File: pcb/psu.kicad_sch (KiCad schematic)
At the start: 20 parts, among them IC3 TPS561243DRLR, IC4 TPS561243DRLR, J1 Conn_01x02_Socket

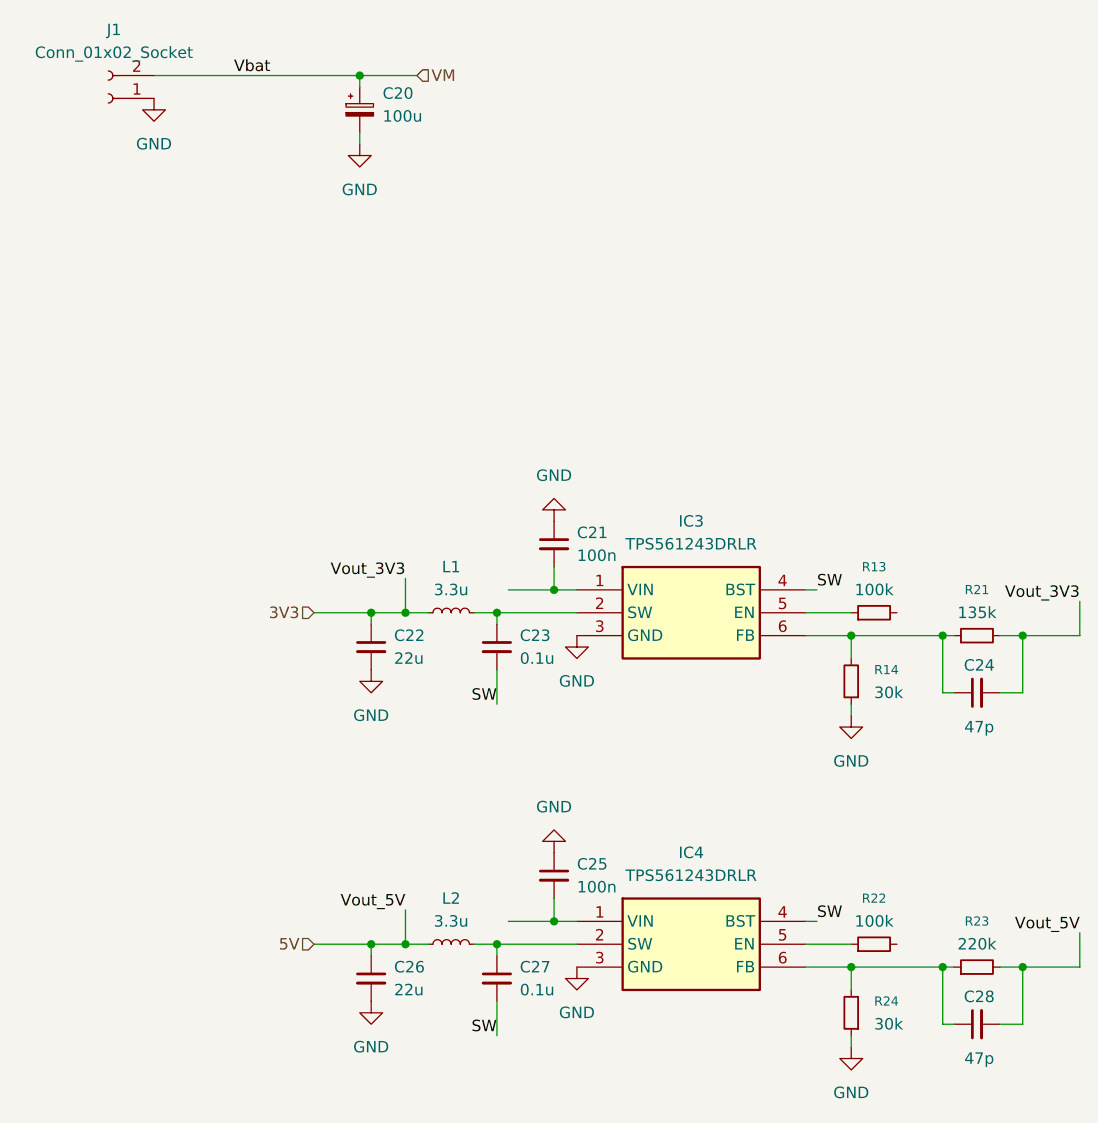
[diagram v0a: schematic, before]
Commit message: driver and buck converter layout
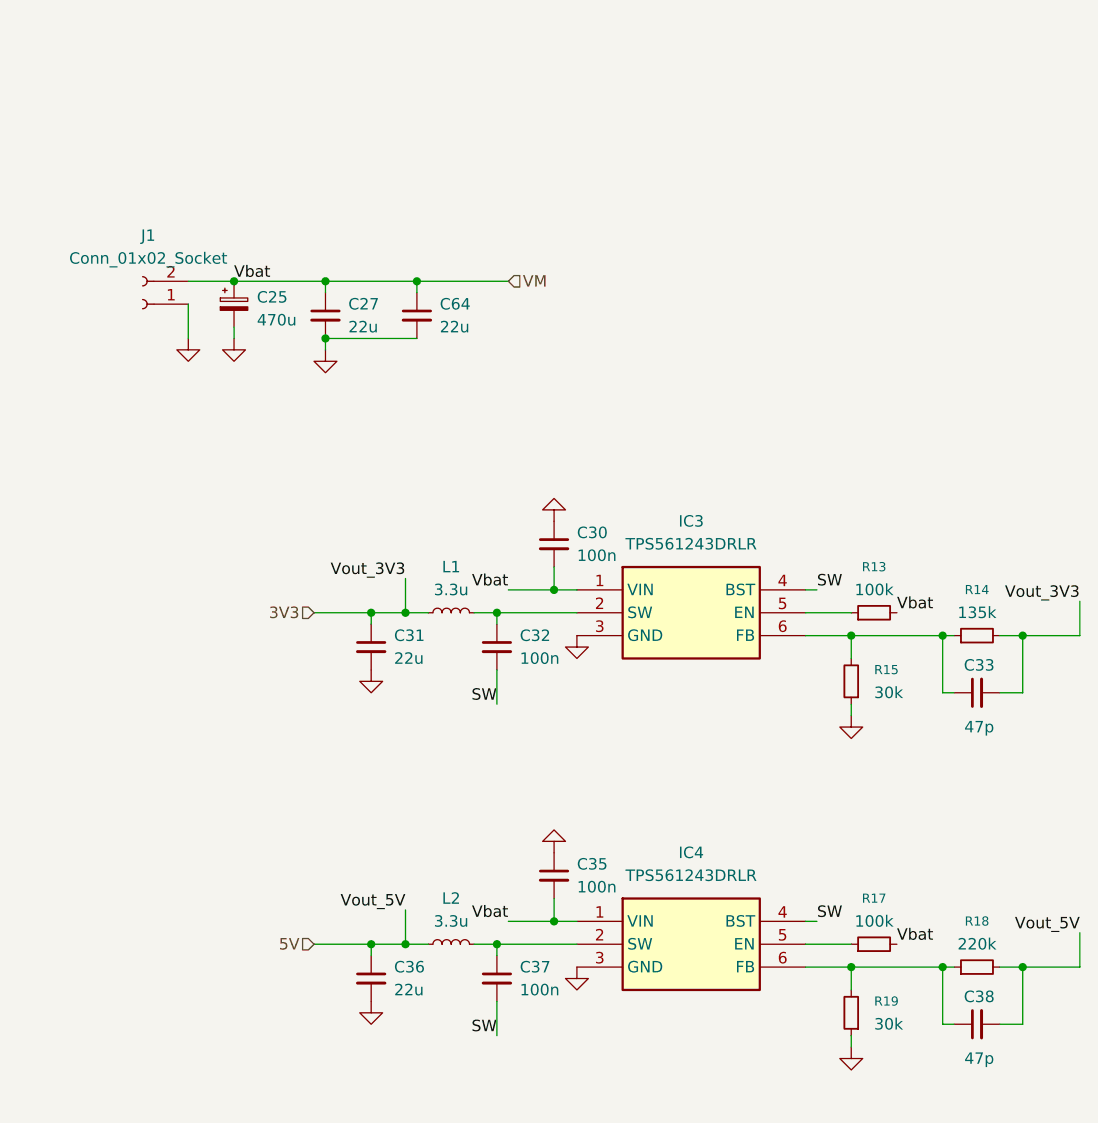
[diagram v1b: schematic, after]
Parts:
- added C27, C64: 22u, Capacitor_SMD:C_0603_1608Metric, symbol Device:C_Small
- C25: renamed from C20; value 100u -> 470u; footprint (none) -> Capacitor_THT:C_Radial_D10.0mm_H16.0mm_P5.00mm
- C30: renamed from C21; footprint (none) -> Capacitor_SMD:C_0603_1608Metric
- C31: renamed from C22; footprint (none) -> Capacitor_SMD:C_0805_2012Metric
- C32: renamed from C23; value 0.1u -> 100n; footprint (none) -> Capacitor_SMD:C_0603_1608Metric
- C33: renamed from C24; footprint (none) -> Capacitor_SMD:C_0603_1608Metric
- C35: renamed from C25; footprint (none) -> Capacitor_SMD:C_0603_1608Metric
- C36: renamed from C26; footprint (none) -> Capacitor_SMD:C_0805_2012Metric
- C37: renamed from C27; value 0.1u -> 100n; footprint (none) -> Capacitor_SMD:C_0603_1608Metric
- C38: renamed from C28; footprint (none) -> Capacitor_SMD:C_0603_1608Metric
- IC3, IC4: footprint SOTFL50P160X60-6N -> TPS561243:SOTFL50P160X60-6N
- J1: footprint (none) -> Connector_AMASS:AMASS_XT60-M_1x02_P7.20mm_Vertical
- L1, L2: footprint (none) -> Inductor_SMD:L_1008_2520Metric
- R13: footprint (none) -> Resistor_SMD:R_0603_1608Metric
- R14: renamed from R21; footprint (none) -> Resistor_SMD:R_0603_1608Metric
- R15: renamed from R14; footprint (none) -> Resistor_SMD:R_0603_1608Metric
- R17: renamed from R22; footprint (none) -> Resistor_SMD:R_0603_1608Metric
- R18: renamed from R23; footprint (none) -> Resistor_SMD:R_0603_1608Metric
- R19: renamed from R24; footprint (none) -> Resistor_SMD:R_0603_1608Metric
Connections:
- net GND: now also C27.2, C64.2
- net VM: now also C30.2, C35.2, IC3.1 (VIN), IC4.1 (VIN), R13.2, R17.2, C27.1, C64.1
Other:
- moved on the sheet: C25, J1

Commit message: routing
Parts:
- J1: footprint Connector_AMASS:AMASS_XT60-M_1x02_P7.20mm_Vertical -> Connector_AMASS:AMASS_XT60PW-M_1x02_P7.20mm_Horizontal
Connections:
- net SW renamed SW3V3
- net SW3V3: no longer C37.2, IC4.4 (BST)
- new net SW5V: C37.2, IC4.4 (BST)
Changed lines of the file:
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@@
-		)
-	)
-	(label "SW"
-		(at 77.47 109.22 180)
-		(effects
-			(font
-				(size 1.27 1.27)
-			)
-			(justify right bottom)
 		)
 	)
@@
 		)
 	)
-	(label "SW"
+	(label "SW5V"
 		(at 113.03 133.35 0)
 		(effects
@@
 		)
 	)
-	(label "SW"
+	(label "SW3V3"
 		(at 113.03 96.52 0)
 		(effects
@@
 		)
 	)
-	(label "SW"
-		(at 77.47 146.05 180)
+	(label "SW5V"
+		(at 77.47 146.05 0)
 		(effects
 			(font
 				(size 1.27 1.27)
 			)
-			(justify right bottom)
+			(justify left bottom)
+		)
+	)
+	(label "SW3V3"
+		(at 77.47 109.22 0)
+		(effects
+			(font
+				(size 1.27 1.27)
+			)
+			(justify left bottom)
 		)
 	)
@@
 		(lib_id "Device:C_Small")
 		(at 83.82 128.27 0)
-		(unit 1)
-		(exclude_from_sim no)
-		(in_bom yes)
-		(on_board yes)
-		(dnp no)
-		(fields_autoplaced yes)
+		(mirror y)
+		(unit 1)
+		(exclude_from_sim no)
+		(in_bom yes)
+		(on_board yes)
+		(dnp no)
 		(property "Reference" "C35"
-			(at 86.36 127.0062 0)
+			(at 81.28 127.0062 0)
 			(effects
 				(font
@@
 		)
 		(property "Value" "100n"
-			(at 86.36 129.5462 0)
+			(at 81.28 129.5462 0)
 			(effects
 				(font
@@
 			)
 		)
-		(property "Footprint" "Connector_AMASS:AMASS_XT60-M_1x02_P7.20mm_Vertical"
+		(property "Footprint" "Connector_AMASS:AMASS_XT60PW-M_1x02_P7.20mm_Horizontal"
 			(at 38.1 64.77 0)
 			(effects

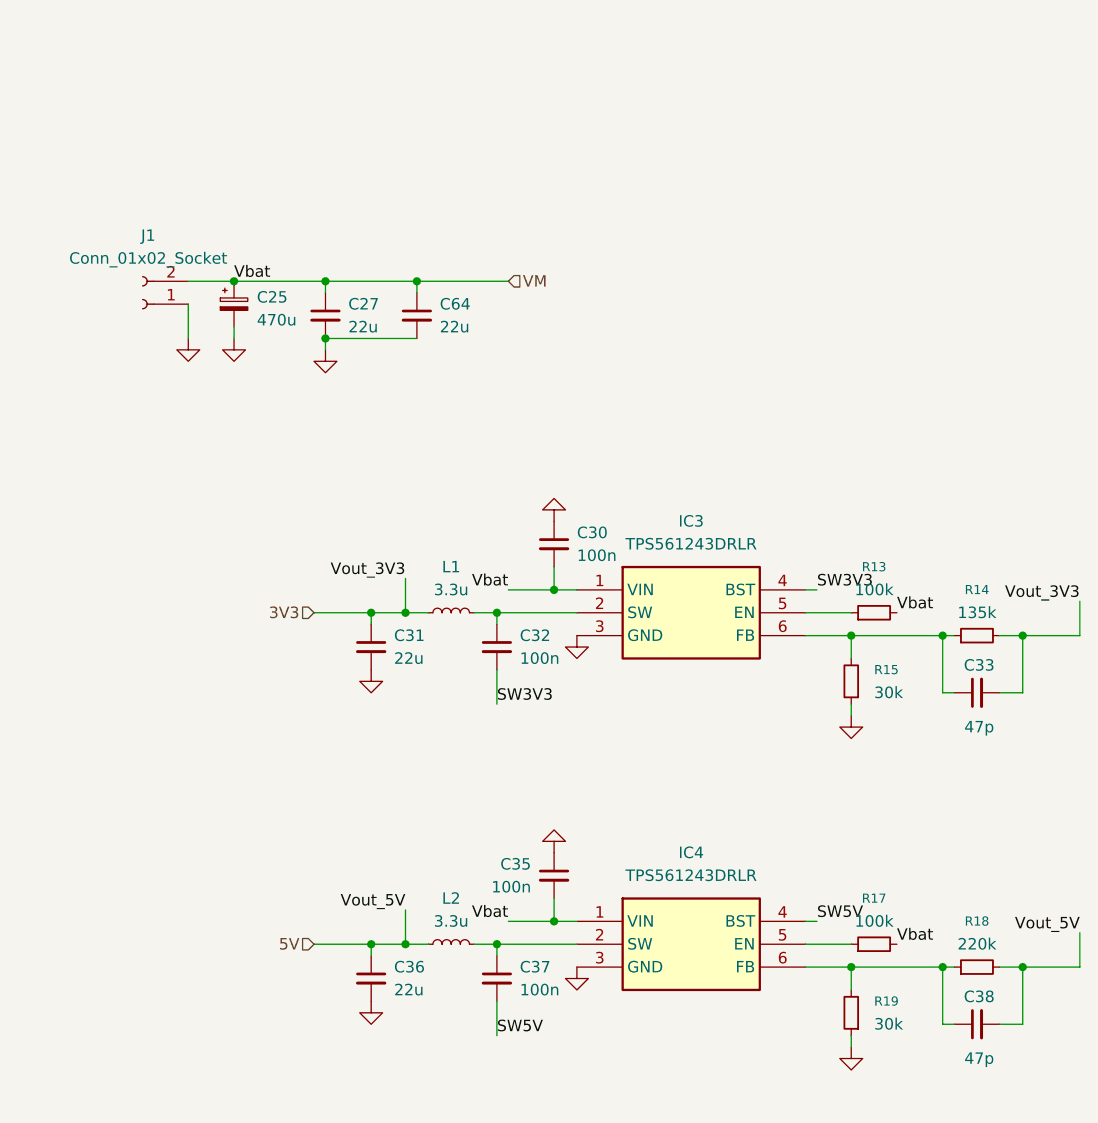
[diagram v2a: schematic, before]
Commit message: add jlcpcb part numbers
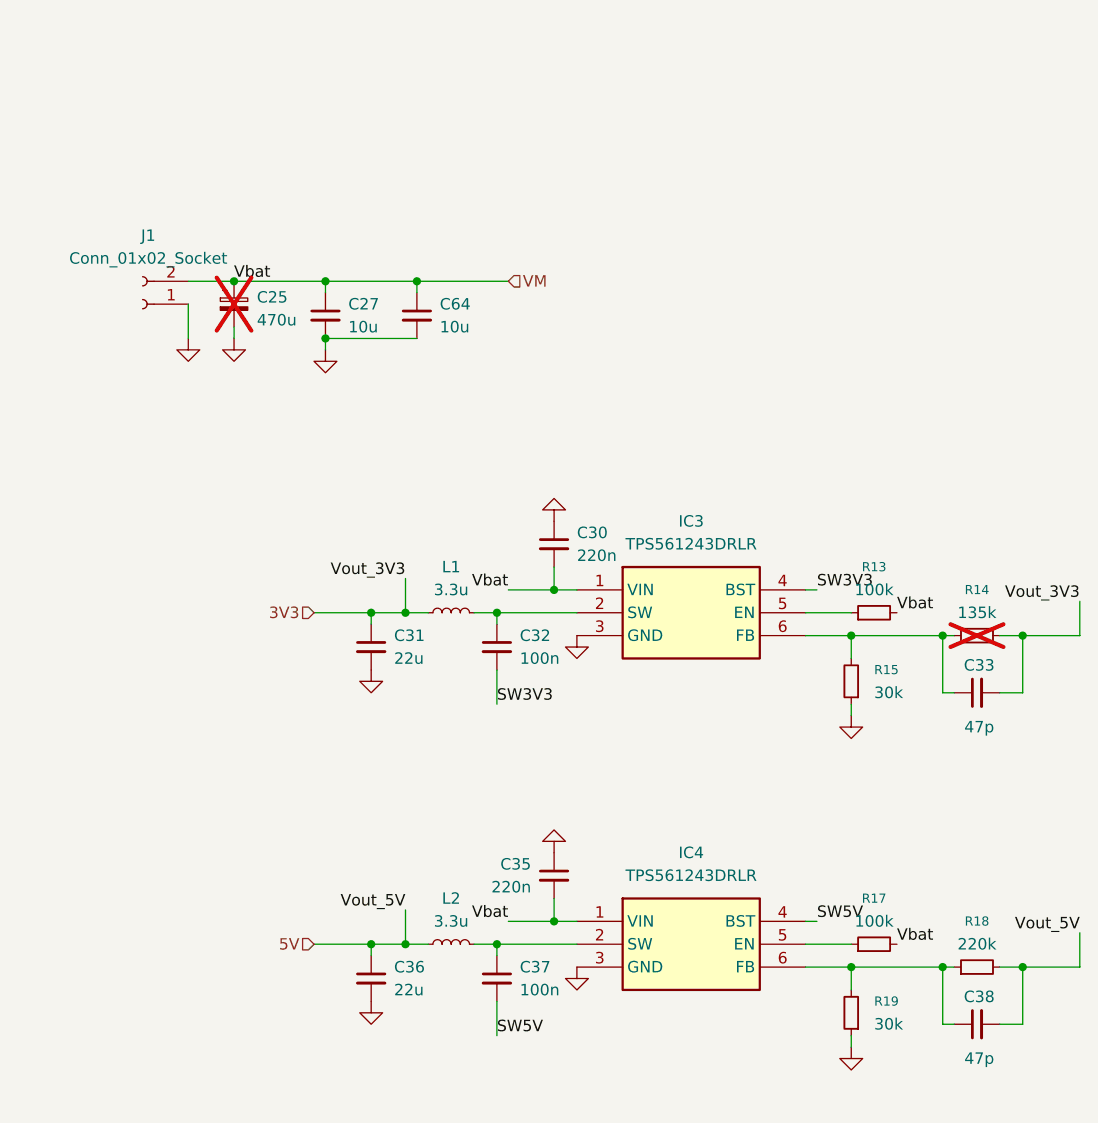
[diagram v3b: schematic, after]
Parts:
- C25, R14: now not fitted
- C27, C64: value 22u -> 10u; JLCPCB Part (none) -> C96446
- C30, C35: value 100n -> 220n; JLCPCB Part (none) -> C21120
- C31, C36: JLCPCB Part (none) -> C45783
- C32, C37: JLCPCB Part (none) -> C14663
- C33, C38: JLCPCB Part (none) -> C1671
- IC3, IC4: JLCPCB Part (none) -> C42040978
- J1: JLCPCB Part (none) -> C98732
- L1, L2: JLCPCB Part (none) -> C5832373
- R13, R17: JLCPCB Part (none) -> C25803
- R15, R19: JLCPCB Part (none) -> C22984
- R18: JLCPCB Part (none) -> C22961
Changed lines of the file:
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@@
 		(in_bom yes)
 		(on_board yes)
-		(dnp no)
+		(dnp yes)
 		(fields_autoplaced yes)
 		(property "Reference" "R14"
@@
 		(property "Description" "Resistor, small symbol"
 			(at 130.81 101.6 0)
+			(effects
+				(font
+					(size 1.27 1.27)
+				)
+				(hide yes)
+			)
+		)
+		(property "JLCPCB Part" ""
+			(at 130.81 101.6 90)
 			(effects
 				(font
@@
 			)
 		)
-		(property "Value" "100n"
+		(property "Value" "220n"
 			(at 81.28 129.5462 0)
 			(effects
@@
 			)
 		)
+		(property "JLCPCB Part" "C21120"
+			(at 83.82 128.27 0)
+			(effects
+				(font
+					(size 1.27 1.27)
+				)
+				(hide yes)
+			)
+		)
 		(pin "1"
 		)
@@
 			)
 		)
+		(property "JLCPCB Part" "C25803"
+			(at 119.38 135.89 90)
+			(effects
+				(font
+					(size 1.27 1.27)
+				)
+				(hide yes)
+			)
+		)
 		(pin "1"
 		)
@@
 			)
 		)
-		(property "Value" "100n"
+		(property "Value" "220n"
 			(at 86.36 92.7162 0)
 			(effects
@@
 			)
 		)
+		(property "JLCPCB Part" "C21120"
+			(at 83.82 91.44 0)
+			(effects
+				(font
+					(size 1.27 1.27)
+				)
+				(hide yes)
+			)
+		)
 		(pin "1"
 		)
@@
 			)
 		)
+		(property "JLCPCB Part" "C5832373"
+			(at 72.39 135.89 90)
+			(effects
+				(font
+					(size 1.27 1.27)
+				)
+				(hide yes)
+			)
+		)
 		(pin "2"
 		)
@@
 			)
 		)
+		(property "JLCPCB Part" "C22961"
+			(at 130.81 138.43 90)
+			(effects
+				(font
+					(size 1.27 1.27)
+				)
+				(hide yes)
+			)
+		)
 		(pin "1"
 		)
@@
 			)
 		)
+		(property "JLCPCB Part" "C1671"
+			(at 130.81 107.95 90)
+			(effects
+				(font
+					(size 1.27 1.27)
+				)
+				(hide yes)
+			)
+		)
 		(pin "1"
 		)
@@
 			)
 		)
+		(property "JLCPCB Part" "C25803"
+			(at 119.38 99.06 90)
+			(effects
+				(font
+					(size 1.27 1.27)
+				)
+				(hide yes)
+			)
+		)
 		(pin "1"
 		)
@@
 			)
 		)
-		(property "Value" "22u"
+		(property "Value" "10u"
 			(at 71.12 67.3162 0)
 			(effects
@@
 			)
 		)
+		(property "JLCPCB Part" "C96446"
+			(at 68.58 66.04 0)
+			(effects
+				(font
+					(size 1.27 1.27)
+				)
+				(hide yes)
+			)
+		)
 		(pin "1"
 		)
@@
 			)
 		)
+		(property "JLCPCB Part" "C42040978"
+			(at 86.36 133.35 0)
+			(effects
+				(font
+					(size 1.27 1.27)
+				)
+				(hide yes)
+			)
+		)
 		(pin "3"
 		)
@@
 			)
 		)
+		(property "JLCPCB Part" "C14663"
+			(at 77.47 139.7 0)
+			(effects
+				(font
+					(size 1.27 1.27)
+				)
+				(hide yes)
+			)
+		)
 		(pin "1"
 		)
@@
 			)
 		)
+		(property "JLCPCB Part" "C5832373"
+			(at 72.39 99.06 90)
+			(effects
+				(font
+					(size 1.27 1.27)
+				)
+				(hide yes)
+			)
+		)
 		(pin "2"
 		)
@@
 			)
 		)
+		(property "JLCPCB Part" "C42040978"
+			(at 86.36 96.52 0)
+			(effects
+				(font
+					(size 1.27 1.27)
+				)
+				(hide yes)
+			)
+		)
 		(pin "3"
 		)
@@
 			)
 		)
+		(property "JLCPCB Part" "C98732"
+			(at 38.1 64.77 0)
+			(effects
+				(font
+					(size 1.27 1.27)
+				)
+				(hide yes)
+			)
+		)
 		(pin "1"
 		)
@@
 			)
 		)
+		(property "JLCPCB Part" "C22984"
+			(at 116.84 143.51 0)
+			(effects
+				(font
+					(size 1.27 1.27)
+				)
+				(hide yes)
+			)
+		)
 		(pin "1"
 		)
@@
 			)
 		)
+		(property "JLCPCB Part" "C45783"
+			(at 63.5 139.7 0)
+			(effects
+				(font
+					(size 1.27 1.27)
+				)
+				(hide yes)
+			)
+		)
 		(pin "1"
 		)
@@
 			)
 		)
-		(property "Value" "22u"
+		(property "Value" "10u"
 			(at 60.96 67.3162 0)
 			(effects
@@
 			)
 		)
+		(property "JLCPCB Part" "C96446"
+			(at 58.42 66.04 0)
+			(effects
+				(font
+					(size 1.27 1.27)
+				)
+				(hide yes)
+			)
+		)
 		(pin "1"
 		)
@@
 			)
 		)
+		(property "JLCPCB Part" "C22984"
+			(at 116.84 106.68 0)
+			(effects
+				(font
+					(size 1.27 1.27)
+				)
+				(hide yes)
+			)
+		)
 		(pin "1"
 		)
@@
 			)
 		)
+		(property "JLCPCB Part" "C45783"
+			(at 63.5 102.87 0)
+			(effects
+				(font
+					(size 1.27 1.27)
+				)
+				(hide yes)
+			)
+		)
 		(pin "1"
 		)
@@
 			)
 		)
+		(property "JLCPCB Part" "C14663"
+			(at 77.47 102.87 0)
+			(effects
+				(font
+					(size 1.27 1.27)
+				)
+				(hide yes)
+			)
+		)
 		(pin "1"
 		)
@@
 			)
 		)
+		(property "JLCPCB Part" "C1671"
+			(at 130.81 144.78 90)
+			(effects
+				(font
+					(size 1.27 1.27)
+				)
+				(hide yes)
+			)
+		)
 		(pin "1"
 		)
@@
 		(in_bom yes)
 		(on_board yes)
-		(dnp no)
+		(dnp yes)
 		(property "Reference" "C25"
 			(at 50.8 64.008 0)
@@
 			(at 48.26 64.77 0)
 			(effects
+				(font
+					(size 1.27 1.27)
+				)
+				(hide yes)
+			)
+		)
+		(property "JLCPCB Part" ""
+			(at 48.26 64.77 0)
+			(effects

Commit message: change layout of extern led board to not show vias
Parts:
- J1: footprint Connector_AMASS:AMASS_XT60PW-M_1x02_P7.20mm_Horizontal -> Equilibot:AMASS_XT60PW-M_1x02_P7.20mm_Horizontal
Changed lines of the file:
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@@
 			)
 		)
-		(property "Footprint" "Connector_AMASS:AMASS_XT60PW-M_1x02_P7.20mm_Horizontal"
+		(property "Footprint" "Equilibot:AMASS_XT60PW-M_1x02_P7.20mm_Horizontal"
 			(at 38.1 64.77 0)
 			(effects

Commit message: PRODUCTION
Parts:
- J1: now not fitted
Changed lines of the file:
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@@
 		(in_bom yes)
 		(on_board yes)
-		(dnp no)
+		(dnp yes)
 		(fields_autoplaced yes)
 		(property "Reference" "J1"
